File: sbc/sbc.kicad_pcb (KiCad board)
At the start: 2 copper layers, 111.8 x 78.7 mm, 23 parts, among them J1 USB_B_Micro, J2 PB, J3 PA, M1 M2.5, M2 M2.5, M3 M2.5, M4 M2.5, SW1 RESET, U1 DS1813, U2 WD65C02, U3 28C256, U4 HM62256BLP, U5 WD65C22, U6 7400, X1 CXO_DIP14

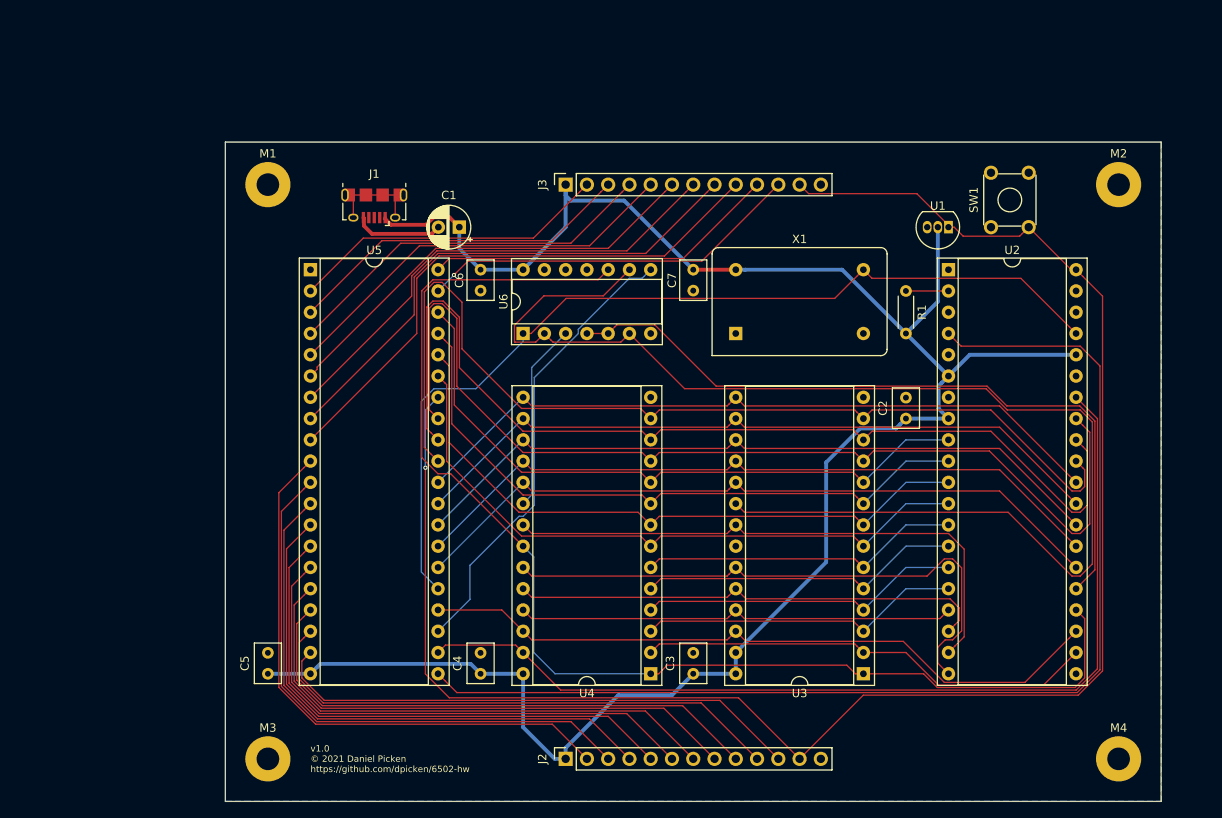
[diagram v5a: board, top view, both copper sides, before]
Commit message: SBC: Fix v1.0 errata
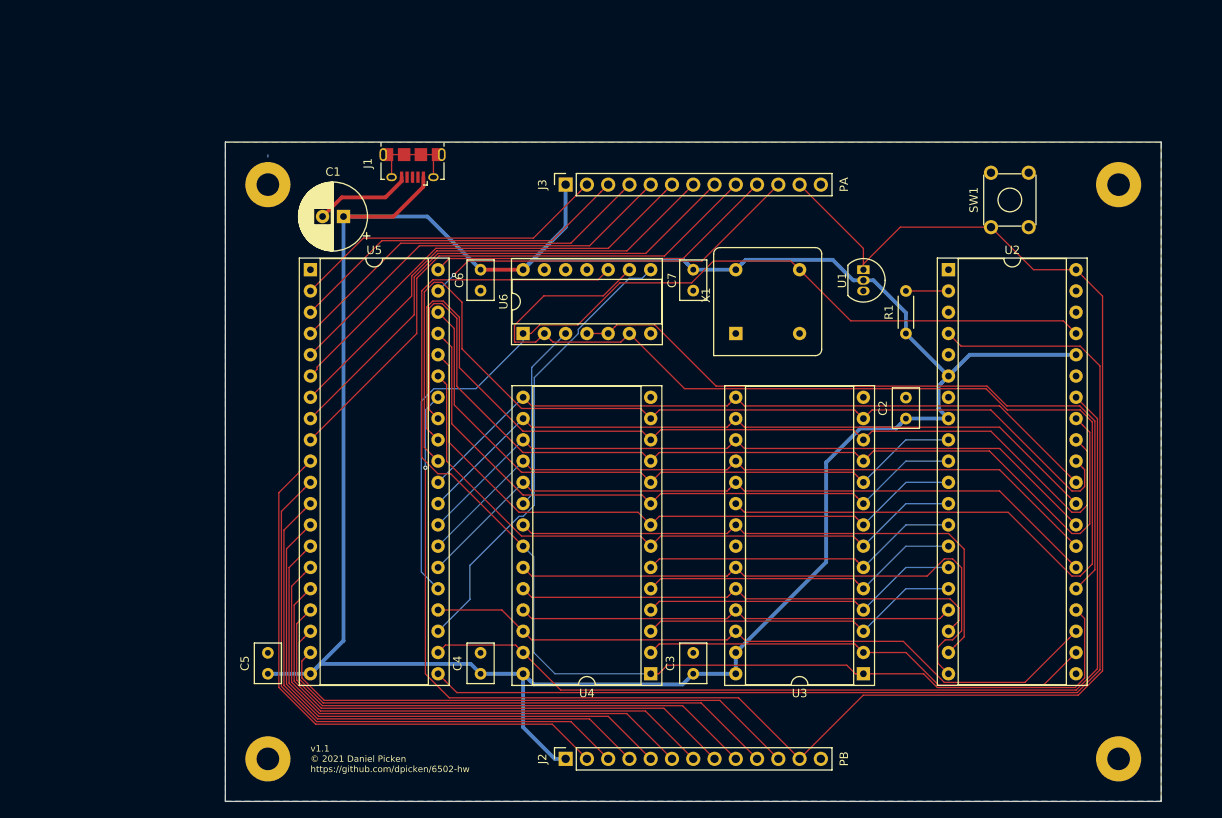
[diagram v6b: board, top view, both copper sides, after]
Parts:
- C1: value 100uf -> 220uf; footprint capacitor:CP_Radial_D5.0mm_P2.50mm -> capacitor:CP_Radial_D8.0mm_P2.50mm
- U4: value HM62256BLP -> 62256
- X1: value CXO_DIP14 -> 2Mhz; footprint oscillator:Oscillator_DIP-14 -> oscillator:Oscillator_DIP-8
- moved C1 13.9 mm to (105.5, 62.2)
- moved U1 11.4 mm to (167.6, 68.6), turned to 270 degrees
- moved J1 6.64 mm to (113.8, 56.1)
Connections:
- C1 pad 2: Net-(C1-Pad2) -> GND
- J1 pad 2: Net-(J1-Pad2) -> (no net)
- J1 pad 3: Net-(J1-Pad3) -> (no net)
- J1 pad 4: Net-(J1-Pad4) -> (no net)
- J1 pad 5: Net-(C1-Pad2) -> GND
- SW1 pad 1: Net-(SW1-Pad1) -> Net-(J2-Pad12)
- SW1 pad 2: Net-(SW1-Pad2) -> (no net)
- SW1 pad 3: Net-(J2-Pad12) -> GND
- SW1 pad 4: GND -> (no net)
- U2 pad 1: Net-(U2-Pad1) -> (no net)
- U2 pad 3: Net-(U2-Pad3) -> (no net)
- U2 pad 35: Net-(U2-Pad35) -> (no net)
- U2 pad 38: Net-(U2-Pad38) -> (no net)
- U2 pad 39: Net-(U2-Pad39) -> (no net)
- U2 pad 5: Net-(U2-Pad5) -> (no net)
- U2 pad 7: Net-(U2-Pad7) -> (no net)
- U6 pad 11: Net-(U6-Pad11) -> (no net)
- X1 pad 8: Net-(U2-Pad37) -> +5V
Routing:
- net +5V: track 242.5 -> 304.0 mm
- net GND: track 0.00 -> 11.7 mm
- net Net-(C1-Pad2): track 10.6 -> 0.00 mm
- net Net-(J2-Pad12): track 210.6 -> 216.2 mm
- net Net-(J1-Pad6): track 11.5 -> 12.7 mm
- net Net-(U2-Pad37): track 111.6 -> 112.5 mm
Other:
- board text added: "v1.1 © 2021 Daniel Picken https://github.com/dpicken/6502-hw"
- board text removed: "v1.0 © 2021 Daniel Picken https://github.com/dpicken/6502-hw"

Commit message: SBC v2.0
Changes:

 - Second VIA
 - NMI button (hardware debounced)
 - 5 status LEDs (power and each VIA port)
 - Ground and power planes
 - Smaller footprint RAM and oscillator
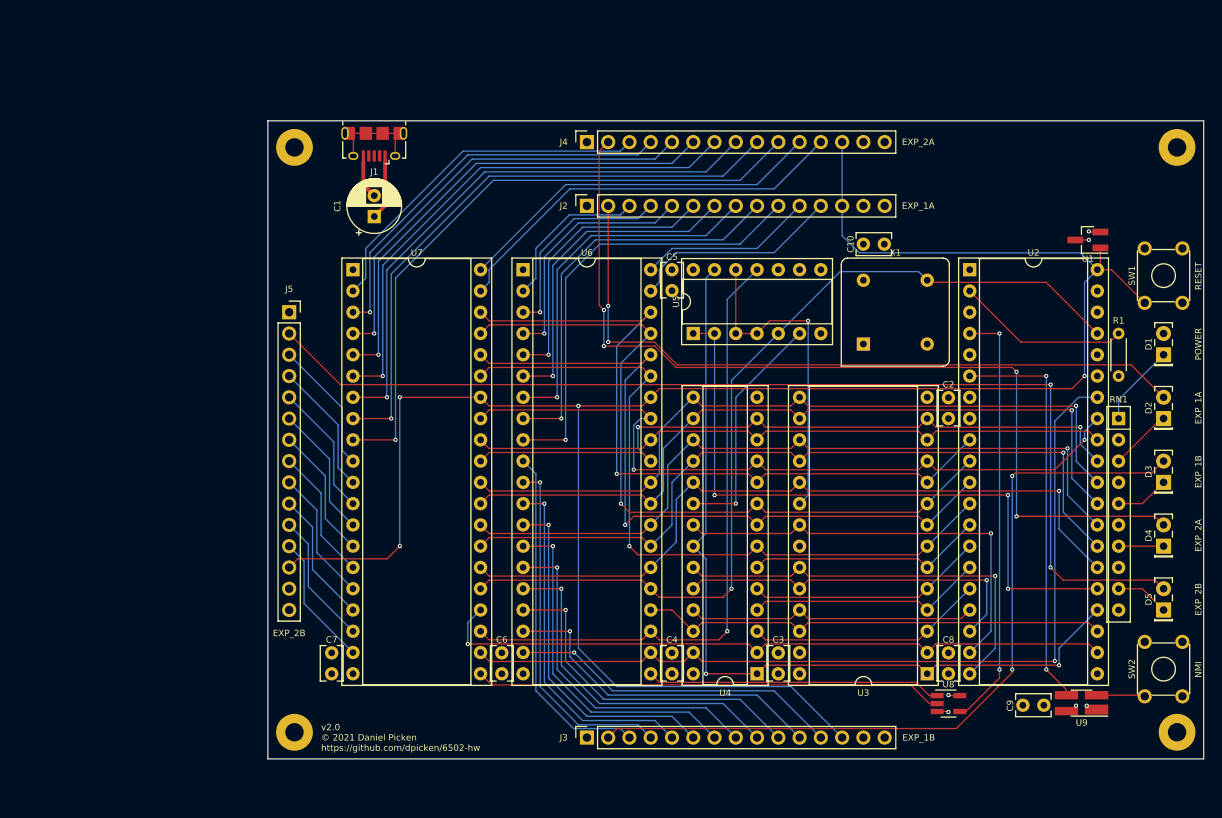
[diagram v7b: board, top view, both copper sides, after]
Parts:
- added C10: 0.1uF, capacitor:C_Rect_L4.0mm_W2.5mm_P2.50mm, F.Cu at (167.6, 65.5)
- added C8: 0.1uF, capacitor:C_Rect_L4.0mm_W2.5mm_P2.50mm, F.Cu at (177.8, 116.8)
- added C9: 0.1uF, capacitor:C_Rect_L4.0mm_W2.5mm_P2.50mm, F.Cu at (189.2, 120.6)
- added D1: POWER, led:LED_Rectangular_W5.0mm_H2.0mm, F.Cu at (203.5, 78.7)
- added D2: EXP_1A, led:LED_Rectangular_W5.0mm_H2.0mm, F.Cu at (203.5, 86.4)
- added D3: EXP_1B, led:LED_Rectangular_W5.0mm_H2.0mm, F.Cu at (203.5, 94.0)
- added D4: EXP_2A, led:LED_Rectangular_W5.0mm_H2.0mm, F.Cu at (203.5, 101.6)
- added D5: EXP_2B, led:LED_Rectangular_W5.0mm_H2.0mm, F.Cu at (203.5, 109.2)
- added J4: EXP_2A, connector:PinSocket_1x15_P2.54mm_Vertical, F.Cu at (134.6, 53.3)
- added J5: EXP_2B, connector:PinSocket_1x15_P2.54mm_Vertical, F.Cu at (99.1, 73.7)
- added RN1: 100, resistor:R_Array_SIP10, F.Cu at (198.1, 86.4)
- added SW2: NMI, switch:SW_TH_Tactile_Omron_B3F-10xx, F.Cu at (201.2, 119.5)
- added U7: WD65C22, dip:DIP-40_W15.24mm_Socket, F.Cu at (106.7, 68.6)
- added U8: 74AHC1G08, to_sot_smd:SOT-23-5_HandSoldering, F.Cu at (177.8, 120.4)
- added U9: MAX6816, to_sot_smd:SOT-143_Handsoldering, F.Cu at (193.7, 120.3)
- C1: footprint capacitor:CP_Radial_D8.0mm_P2.50mm -> capacitor:CP_Radial_D6.3mm_P2.50mm
- C2, C3, C4, C5, C6, C7: footprint capacitor:C_Rect_L4.6mm_W3.0mm_P2.50mm_MKS02_FKP02 -> capacitor:C_Rect_L4.0mm_W2.5mm_P2.50mm
- J1: footprint connector_usb:USB_Micro-B_Amphenol_10118194_Horizontal -> connector_usb_handsoldering:USB_Micro-B_Amphenol_10118194_Horizontal_HandSoldering
- J2: value PB -> EXP_1A; footprint connector:PinSocket_1x13_P2.54mm_Vertical -> connector:PinSocket_1x15_P2.54mm_Vertical
- J3: value PA -> EXP_1B; footprint connector:PinSocket_1x13_P2.54mm_Vertical -> connector:PinSocket_1x15_P2.54mm_Vertical
- M1, M2, M3, M4: value M2.5 -> M2; footprint mounting_hole:MountingHole_2.7mm_M2.5_Pad -> mounting_hole:MountingHole_2.2mm_M2_Pad
- U1: footprint to_sot:TO-92_Inline -> to_sot_smd:SOT-23_Handsoldering
- U4: footprint dip:DIP-28_W15.24mm_Socket -> dip:DIP-28_W7.62mm_Socket
- U5: value WD65C22 -> 7400; footprint dip:DIP-40_W15.24mm_Socket -> dip:DIP-14_W7.62mm_Socket
- U6: value 7400 -> WD65C22; footprint dip:DIP-14_W7.62mm_Socket -> dip:DIP-40_W15.24mm_Socket
- moved M2 118.2 mm to (99.7, 123.8)
- moved M3 108.6 mm to (205.1, 123.8)
- moved M4 73.4 mm to (205.1, 54.0)
- moved C5 68.2 mm to (144.8, 68.6), turned to 270 degrees
- moved J2 66.1 mm to (134.6, 61.0)
- moved J3 66.1 mm to (134.6, 124.5)
- moved C7 64.8 mm to (104.1, 116.8), turned to 90 degrees
- moved C6 48.3 mm to (124.5, 116.8), turned to 90 degrees
- moved U5 46.4 mm to (147.3, 76.2), turned to 90 degrees
- moved U1 27.0 mm to (194.4, 65.0), turned to 180 degrees
- moved R1 25.9 mm to (198.1, 76.2)
- moved C4 22.9 mm to (144.8, 116.8)
- moved SW1 20.5 mm to (201.2, 72.5)
- moved X1 15.3 mm to (167.6, 77.5)
- moved U4 12.7 mm to (154.9, 116.8)
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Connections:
- J1 pad 2: (no net) -> Net-(J1-Pad2)
- J1 pad 3: (no net) -> Net-(J1-Pad3)
- J1 pad 4: (no net) -> Net-(J1-Pad4)
- J2 pad 10: /CB1 -> VIA1_PA7
- J2 pad 11: /CB2 -> VIA1_CA1
- J2 pad 12: Net-(J2-Pad12) -> VIA1_CA2
- J2 pad 13: GND -> RESET
- J2 pad 2: /PB0 -> EXP_1A_LED
- J2 pad 3: /PB1 -> VIA1_PA0
- J2 pad 4: /PB2 -> VIA1_PA1
- J2 pad 5: /PB3 -> VIA1_PA2
- J2 pad 6: /PB4 -> VIA1_PA3
- J2 pad 7: /PB5 -> VIA1_PA4
- J2 pad 8: /PB6 -> VIA1_PA5
- J2 pad 9: /PB7 -> VIA1_PA6
- J3 pad 10: /CA1 -> VIA1_PB7
- J3 pad 11: /CA2 -> VIA1_CB1
- J3 pad 12: Net-(J2-Pad12) -> VIA1_CB2
- J3 pad 13: GND -> RESET
- J3 pad 2: /PA0 -> EXP_1B_LED
- J3 pad 3: /PA1 -> VIA1_PB0
- J3 pad 4: /PA2 -> VIA1_PB1
- J3 pad 5: /PA3 -> VIA1_PB2
- J3 pad 6: /PA4 -> VIA1_PB3
- J3 pad 7: /PA5 -> VIA1_PB4
- J3 pad 8: /PA6 -> VIA1_PB5
- J3 pad 9: /PA7 -> VIA1_PB6
- SW1 pad 1: Net-(J2-Pad12) -> RESET
- U1 pad 1: Net-(J2-Pad12) -> RESET
- U2 pad 1: (no net) -> Net-(U2-Pad1)
- U2 pad 3: (no net) -> Net-(U2-Pad3)
- U2 pad 35: (no net) -> Net-(U2-Pad35)
- U2 pad 38: (no net) -> Net-(U2-Pad38)
- U2 pad 39: (no net) -> Net-(U2-Pad39)
- U2 pad 4: Net-(U2-Pad4) -> IRQ
- U2 pad 40: Net-(J2-Pad12) -> RESET
- U2 pad 5: (no net) -> Net-(U2-Pad5)
- U2 pad 6: +5V -> NMI
- U2 pad 7: (no net) -> Net-(U2-Pad7)
- U5 pad 1: GND -> /A15
- U5 pad 10: /PB0 -> GND
- U5 pad 11: /PB1 -> Net-(U5-Pad11)
- U5 pad 12: /PB2 -> Net-(U3-Pad20)
- U5 pad 13: /PB3 -> /A14
- U5 pad 14: /PB4 -> +5V
- U5 pad 2: /PA0 -> /A15
- U5 pad 3: /PA1 -> Net-(U3-Pad20)
- U5 pad 4: /PA2 -> Net-(U3-Pad20)
- U5 pad 5: /PA3 -> Net-(U2-Pad37)
- U5 pad 6: /PA4 -> Net-(U4-Pad20)
- U5 pad 7: /PA5 -> GND
- U5 pad 8: /PA6 -> Net-(U5-Pad8)
- U5 pad 9: /PA7 -> GND
- U6 pad 1: Net-(U2-Pad37) -> GND
- U6 pad 10: /A14 -> VIA1_PB0
- U6 pad 11: (no net) -> VIA1_PB1
- U6 pad 12: GND -> VIA1_PB2
- U6 pad 13: GND -> VIA1_PB3
- U6 pad 14: +5V -> VIA1_PB4
- U6 pad 2: Net-(U3-Pad20) -> VIA1_PA0
- U6 pad 3: Net-(U4-Pad20) -> VIA1_PA1
- U6 pad 4: /A15 -> VIA1_PA2
- U6 pad 5: /A15 -> VIA1_PA3
- U6 pad 6: Net-(U3-Pad20) -> VIA1_PA4
- U6 pad 7: GND -> VIA1_PA5
- U6 pad 8: Net-(U5-Pad23) -> VIA1_PA6
- U6 pad 9: Net-(U3-Pad20) -> VIA1_PA7
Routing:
- net +5V: track 304.0 -> 37.3 mm, vias 0 -> 3
- net RESET: track 0.00 -> 247.3 mm, vias 0 -> 4
- net Net-(J2-Pad12): track 216.2 -> 0.00 mm, vias 1 -> 0
- net Net-(U2-Pad4): track 137.1 -> 0.00 mm
- net EXP_2B_LED: track 0.00 -> 129.9 mm, vias 0 -> 2
- net Net-(U3-Pad20): track 156.8 -> 39.7 mm, vias 0 -> 1
- net EXP_2A_LED: track 0.00 -> 110.9 mm, vias 0 -> 4
- net EXP_1B_LED: track 0.00 -> 93.8 mm, vias 0 -> 2
- net EXP_1A_LED: track 0.00 -> 85.3 mm, vias 0 -> 2
- net VIA2_PA7: track 0.00 -> 76.8 mm, vias 0 -> 1
- net Net-(U5-Pad11): track 0.00 -> 75.8 mm, vias 0 -> 1
- net VIA2_PA6: track 0.00 -> 72.1 mm, vias 0 -> 1
- net /PB0: track 68.9 -> 0.00 mm
- net /PB1: track 68.4 -> 0.00 mm
- net /PB2: track 67.9 -> 0.00 mm
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- added copper zone on In1.Cu, net +5V
- added copper zone on In2.Cu, net GND
- removed copper zone on B.Cu, net GND
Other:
- board size 111.8 x 78.7 mm -> 111.8 x 76.2 mm
- copper layers 2 -> 4
- board text added: "v2.0 © 2021 Daniel Picken https://github.com/dpicken/6502-hw"
- board text removed: "v1.1 © 2021 Daniel Picken https://github.com/dpicken/6502-hw"

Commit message: SBC v2.1
Address some v2.0 errata:

  - SBC: Fix LED array layout
  - OLED interposer: Tidy silkscreen
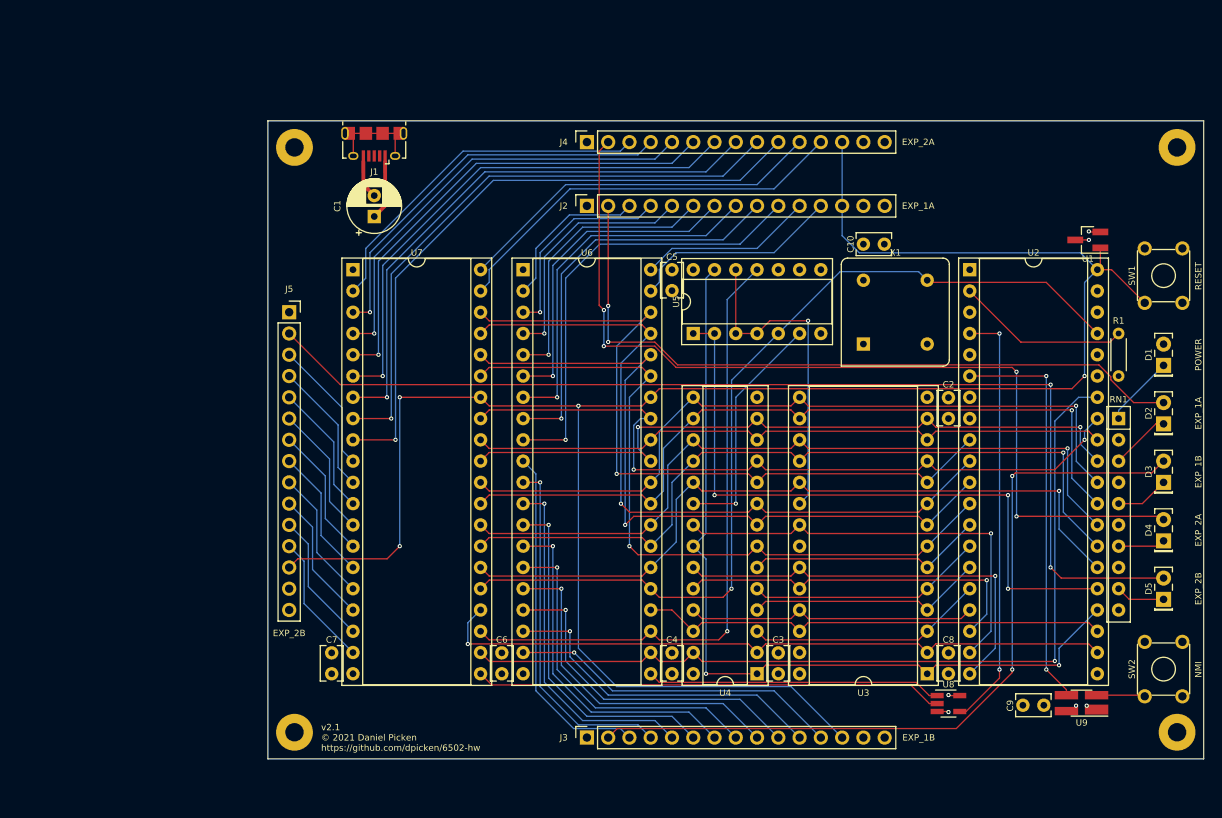
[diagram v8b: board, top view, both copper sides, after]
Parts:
- moved D1 1.27 mm to (203.5, 80.0)
- moved D5 1.27 mm to (203.5, 108.0)
- moved D2 0.64 mm to (203.5, 87.0)
- moved D4 0.63 mm to (203.5, 101.0)
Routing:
- net Net-(D1-Pad1): track 9.84 -> 8.57 mm
- net EXP_2B_LED: track 129.9 -> 129.3 mm
- net Net-(D5-Pad1): track 6.42 -> 5.90 mm
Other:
- board text added: "v2.1 © 2021 Daniel Picken https://github.com/dpicken/6502-hw"
- board text removed: "v2.0 © 2021 Daniel Picken https://github.com/dpicken/6502-hw"
